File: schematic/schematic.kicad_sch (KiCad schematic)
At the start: 25 parts, among them SW1 SW_SPST, U1 ESP32-S3-DevKitC

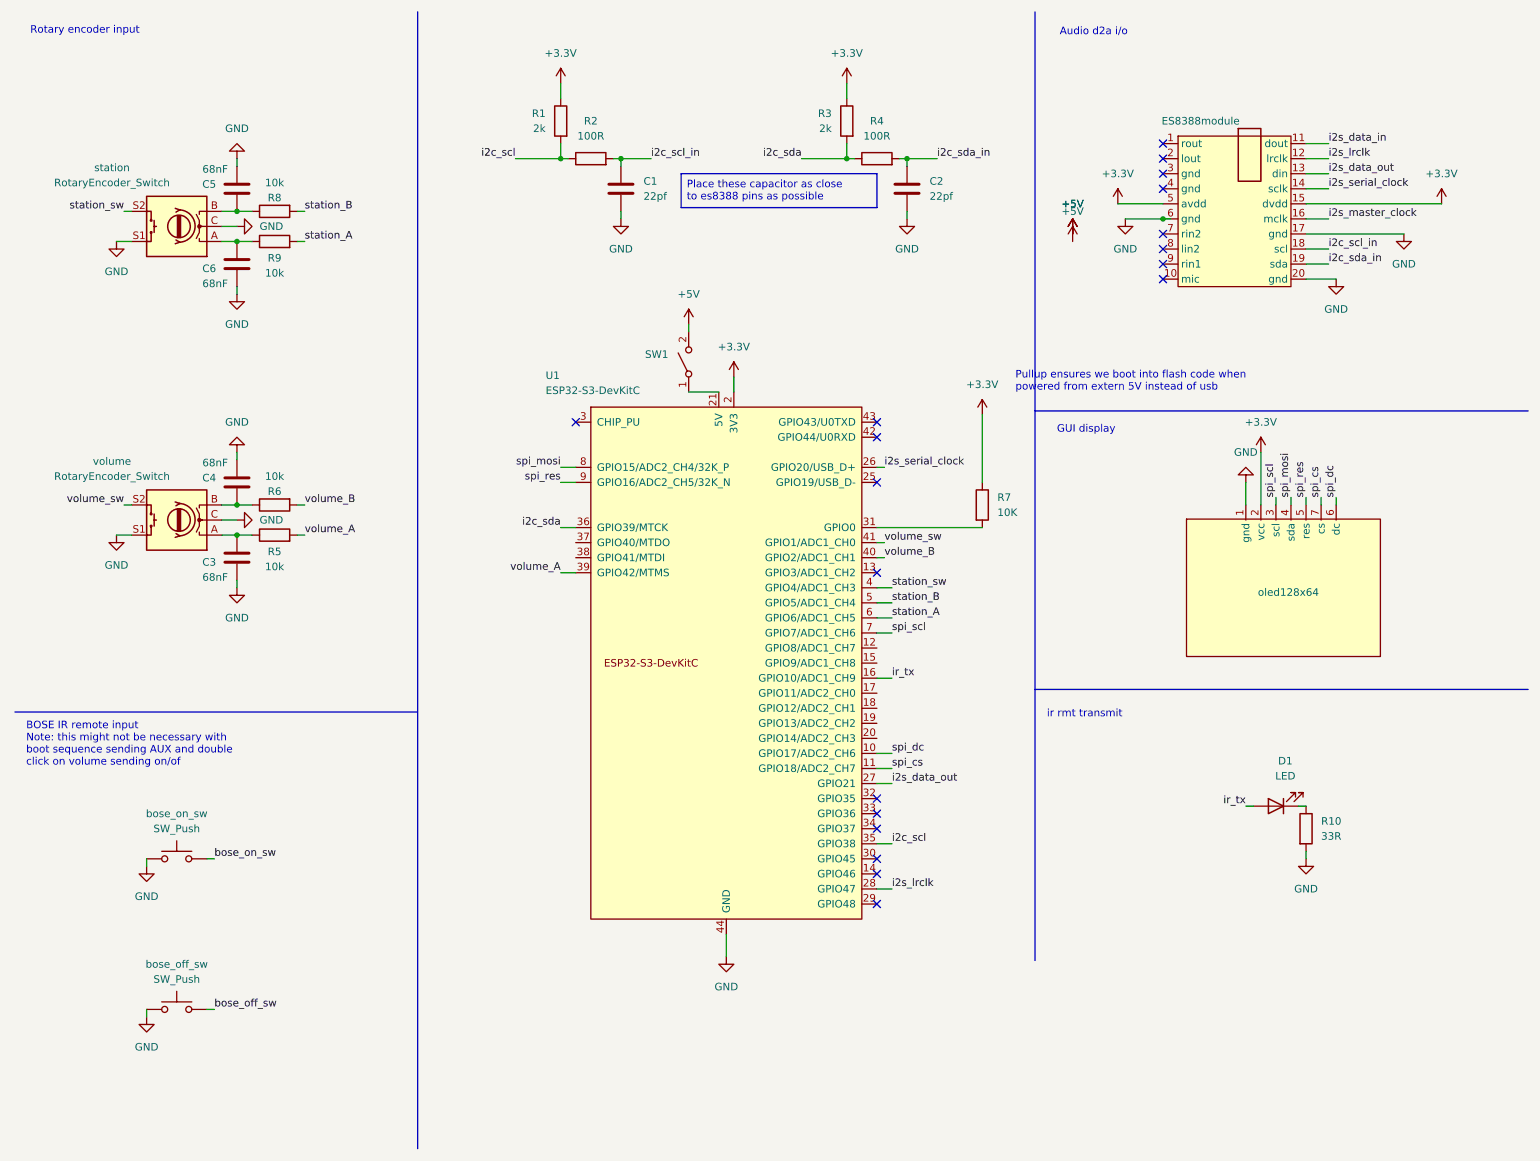
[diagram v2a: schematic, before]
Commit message: Assigned footprints and created custom footprints in prepartion for pcb layout.
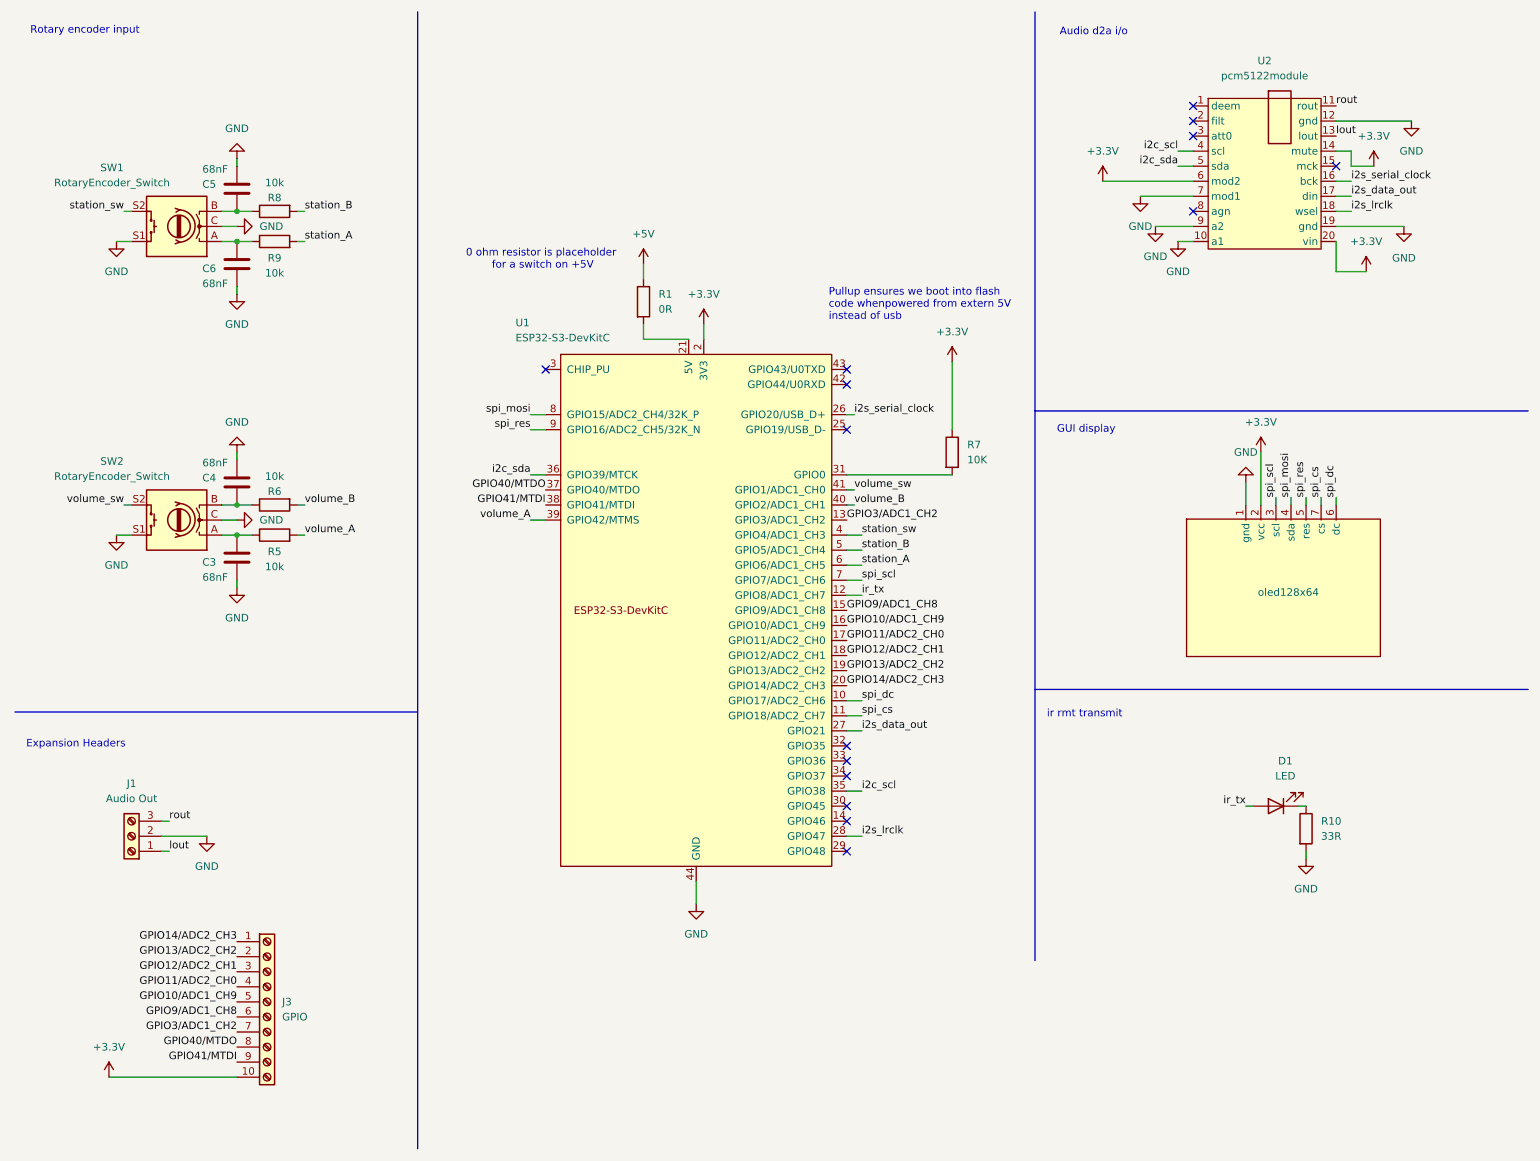
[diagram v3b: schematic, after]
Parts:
- removed C1, C2: 22pf, symbol Device:C
- removed ES8388module: ~, symbol es8388_module:es8388_module
- removed R2, R4: 100R, symbol Device:R
- removed R3: 2k, symbol Device:R
- removed SW1: SW_SPST, symbol Switch:SW_SPST
- removed bose_off_sw, bose_on_sw: SW_Push, symbol Switch:SW_Push
- added J1: Audio Out, TerminalBlock:TerminalBlock_Xinya_XY308-2.54-3P_1x03_P2.54mm_Horizontal, symbol Connector:Screw_Terminal_01x03
- added J3: GPIO, TerminalBlock:TerminalBlock_Xinya_XY308-2.54-10P_1x10_P2.54mm_Horizontal, symbol Connector:Screw_Terminal_01x10
- added U2: pcm5122module, symbol audio_boards:pcm5122
- C3, C4, C5, C6: footprint (none) -> Capacitor_SMD:C_1206_3216Metric_Pad1.33x1.80mm_HandSolder
- D1: footprint (none) -> LED_THT:LED_D3.0mm_IRGrey
- R1: value 2k -> 0R; footprint (none) -> Resistor_THT:R_Axial_DIN0207_L6.3mm_D2.5mm_P7.62mm_Horizontal
- R10, R5, R6, R7, R8, R9: footprint (none) -> Resistor_SMD:R_1206_3216Metric_Pad1.30x1.75mm_HandSolder
- SW1: renamed from station; footprint (none) -> rotary_encoder:XDCR_PEC11R-4220F-S0024
- SW2: renamed from volume; footprint (none) -> rotary_encoder:XDCR_PEC11R-4220F-S0024
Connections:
- net +3.3V: now also J3.10 (Pin_10), U2.14 (mute), U2.20 (vin), U2.6 (mod2); no longer R1.1
- net +5V: now also R1.1
- net GND: now also J1.2 (Pin_2), U2.10 (a1), U2.12 (gnd), U2.19 (gnd), U2.7 (mod1), U2.9 (a2)
- net i2c_scl: now also U2.4 (scl); no longer R1.2
- net i2c_sda: now also U2.5 (sda)
- net i2s_data_out: now also U2.17 (din)
- net i2s_lrclk: now also U2.18 (wsel)
- net i2s_serial_clock: now also U2.16 (bck)
- net ir_tx: now also U1.12 (GPIO8/ADC1_CH7); no longer U1.16 (GPIO10/ADC1_CH9)
- net at U1.21 (5V): now also R1.2
- net GPIO3/ADC1_CH2: now reaches U1.13 (GPIO3/ADC1_CH2)
- net GPIO3/ADC1_CH2: now also J3.7 (Pin_7)
- net GPIO9/ADC1_CH8: now reaches U1.15 (GPIO9/ADC1_CH8)
- net GPIO9/ADC1_CH8: now also J3.6 (Pin_6)
- net GPIO11/ADC2_CH0: now reaches U1.17 (GPIO11/ADC2_CH0)
- net GPIO11/ADC2_CH0: now also J3.4 (Pin_4)
- net GPIO12/ADC2_CH1: now reaches U1.18 (GPIO12/ADC2_CH1)
- net GPIO12/ADC2_CH1: now also J3.3 (Pin_3)
- net GPIO13/ADC2_CH2: now reaches U1.19 (GPIO13/ADC2_CH2)
- net GPIO13/ADC2_CH2: now also J3.2 (Pin_2)
- net GPIO14/ADC2_CH3: now reaches U1.20 (GPIO14/ADC2_CH3)
- net GPIO14/ADC2_CH3: now also J3.1 (Pin_1)
- net GPIO40/MTDO: now reaches U1.37 (GPIO40/MTDO)
- net GPIO40/MTDO: now also J3.8 (Pin_8)
- net GPIO41/MTDI: now reaches U1.38 (GPIO41/MTDI)
- net GPIO41/MTDI: now also J3.9 (Pin_9)
- new net GPIO10/ADC1_CH9: J3.5 (Pin_5), U1.16 (GPIO10/ADC1_CH9)
- new net lout: J1.1 (Pin_1), U2.13 (lout)
- new net rout: J1.3 (Pin_3), U2.11 (rout)
- no-connect marks 19 -> 15
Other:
- note added: "0 ohm resistor is placeholder for a switch on +5V"
- note added: "Expansion Headers"
- note added: "Pullup ensures we boot into flash code whenpowered from extern 5V instead of usb"
- note removed: "BOSE IR remote input Note: this might not be necessary with boot sequence sending AUX and double click on volume sending on/of"
- note removed: "Pullup ensures we boot into flash code when powered from extern 5V instead of usb"
- moved on the sheet: R7, U1

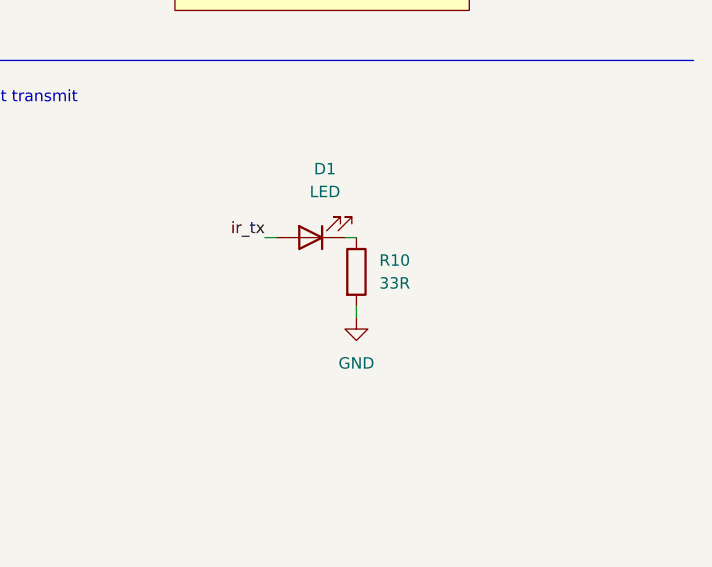
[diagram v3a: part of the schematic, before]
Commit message: Change current limiting resistor to 100R from 33R.  Lower power seems to work fine for the ir remote.
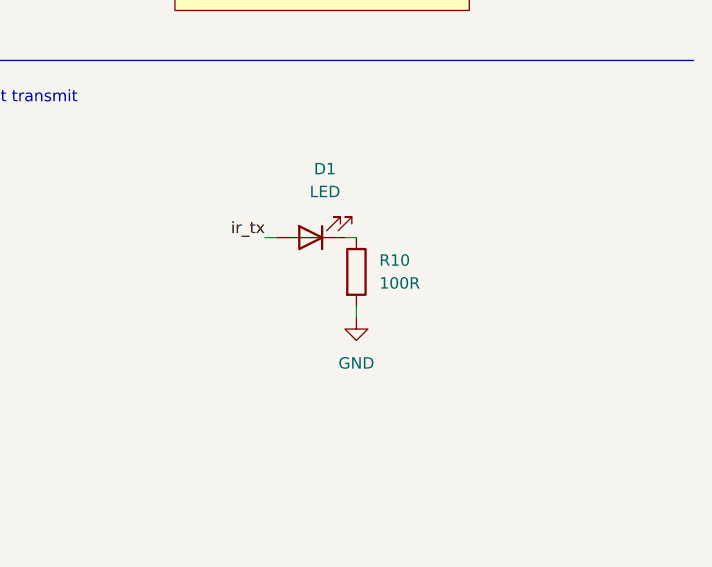
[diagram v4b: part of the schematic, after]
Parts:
- R10: value 33R -> 100R
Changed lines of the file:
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@@
 			)
 		)
-		(property "Value" "33R"
+		(property "Value" "100R"
 			(at 232.41 151.1299 0)
 			(effects

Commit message: Design PCB.
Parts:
- removed R1: 0R, Resistor_THT:R_Axial_DIN0207_L6.3mm_D2.5mm_P7.62mm_Horizontal, symbol Device:R
- removed R5, R6: 10k, Resistor_SMD:R_1206_3216Metric_Pad1.30x1.75mm_HandSolder, symbol Device:R
- removed SW1, SW2: RotaryEncoder_Switch, rotary_encoder:XDCR_PEC11R-4220F-S0024, symbol Device:RotaryEncoder_Switch
- added J3: Conn_01x02, Connector_Wire:SolderWire-0.1sqmm_1x02_P3.6mm_D0.4mm_OD1mm, symbol Connector_Generic:Conn_01x02
- added R3, R4: 10k, Resistor_SMD:R_0805_2012Metric_Pad1.20x1.40mm_HandSolder, symbol Device:R
- added S1, S2: PEC11R-4220F-S0024, rotary_encoder:XDCR_PEC11R-4220F-S0024, symbol rotary_encoder:PEC11R-4220F-S0024
- C1: renamed from C5; footprint Capacitor_SMD:C_1206_3216Metric_Pad1.33x1.80mm_HandSolder -> Capacitor_SMD:C_0805_2012Metric_Pad1.18x1.45mm_HandSolder
- C2: renamed from C6; footprint Capacitor_SMD:C_1206_3216Metric_Pad1.33x1.80mm_HandSolder -> Capacitor_SMD:C_0805_2012Metric_Pad1.18x1.45mm_HandSolder
- C3, C4: footprint Capacitor_SMD:C_1206_3216Metric_Pad1.33x1.80mm_HandSolder -> Capacitor_SMD:C_0805_2012Metric_Pad1.18x1.45mm_HandSolder
- R1: renamed from R8; footprint Resistor_SMD:R_1206_3216Metric_Pad1.30x1.75mm_HandSolder -> Resistor_SMD:R_0805_2012Metric_Pad1.20x1.40mm_HandSolder
- R2: renamed from R9; footprint Resistor_SMD:R_1206_3216Metric_Pad1.30x1.75mm_HandSolder -> Resistor_SMD:R_0805_2012Metric_Pad1.20x1.40mm_HandSolder
- R6: renamed from R7; footprint Resistor_SMD:R_1206_3216Metric_Pad1.30x1.75mm_HandSolder -> Resistor_SMD:R_0805_2012Metric_Pad1.20x1.40mm_HandSolder
- R7: renamed from R10; footprint Resistor_SMD:R_1206_3216Metric_Pad1.30x1.75mm_HandSolder -> Resistor_SMD:R_0805_2012Metric_Pad1.20x1.40mm_HandSolder
- U2: footprint (none) -> audio_boards:pcm5122_module
- oled128x1: renamed from oled128x64; footprint (none) -> oled128x64_spi:oled128x64_spi
- renumbered J3 to J2
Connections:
- net GND: now also J3.2 (Pin_2), S1.1, S1.C (COM), S1.SH1 (SHIELD), S1.SH2 (SHIELD__1), S2.1, S2.C (COM), S2.SH1 (SHIELD), S2.SH2 (SHIELD__1)
- net station_A: now also R1.2, U1.5 (GPIO5/ADC1_CH4); no longer R2.2, U1.6 (GPIO6/ADC1_CH5)
- net station_B: now also R2.2, U1.4 (GPIO4/ADC1_CH3); no longer R1.2, U1.5 (GPIO5/ADC1_CH4)
- net station_sw: now also U1.6 (GPIO6/ADC1_CH5), S1.2; no longer U1.4 (GPIO4/ADC1_CH3)
- net volume_A: now also R3.2
- net volume_B: now also R4.2
- net volume_sw: now also S2.2
- net at U1.21 (5V): now also J3.1 (Pin_1)
- net at C4.1: now also R4.1, S2.B
- net at C2.1, R2.1: now also S1.B
- net at C1.1, R1.1: now also S1.A
- net at C3.1: now also R3.1, S2.A
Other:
- moved on the sheet: C1, C2, R1, R2

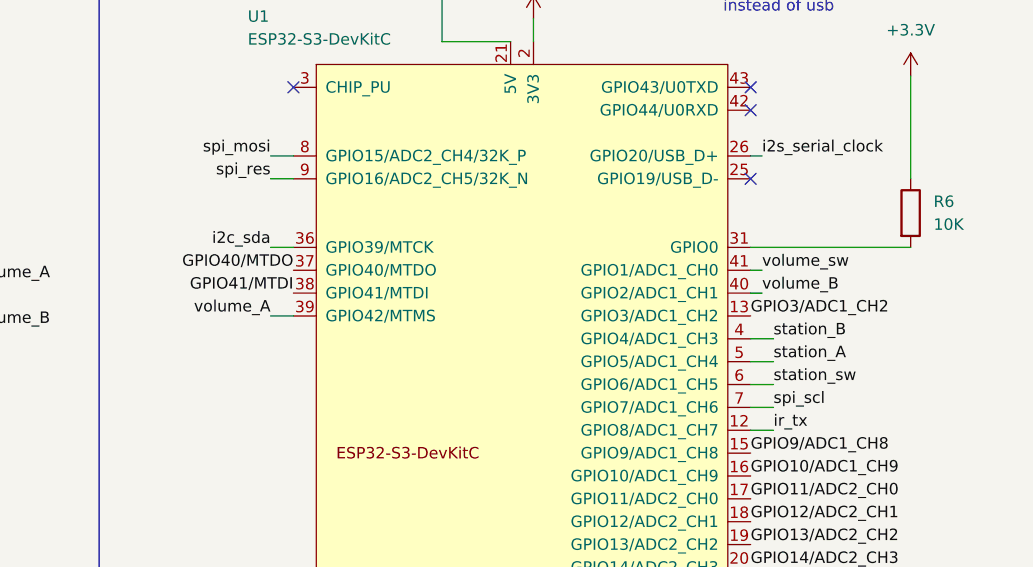
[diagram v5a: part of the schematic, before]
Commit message: Reassigned volume encoder pins in order to reroute outside of the esp32 antenna.  Also added a keep out zone on both top and bottom around the antenna.
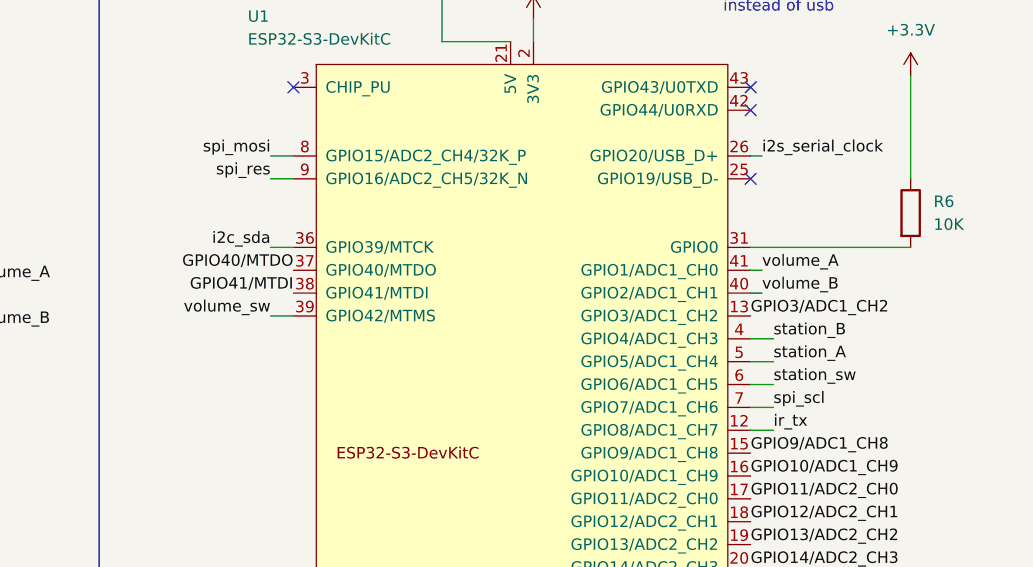
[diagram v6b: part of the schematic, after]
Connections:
- net volume_A: now also U1.41 (GPIO1/ADC1_CH0); no longer U1.39 (GPIO42/MTMS)
- net volume_sw: now also U1.39 (GPIO42/MTMS); no longer U1.41 (GPIO1/ADC1_CH0)
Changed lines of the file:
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@@
-		)
-	)
-	(label "volume_A"
-		(at 99.06 97.79 180)
-		(effects
-			(font
-				(size 1.27 1.27)
-			)
-			(justify right bottom)
 		)
 	)
@@
 		)
 	)
+	(label "volume_A"
+		(at 153.67 92.71 0)
+		(effects
+			(font
+				(size 1.27 1.27)
+			)
+			(justify left bottom)
+		)
+	)
 	(label "GPIO11/ADC2_CH0"
 		(at 152.4 118.11 0)
@@
 	)
 	(label "volume_sw"
-		(at 153.67 92.71 0)
-		(effects
-			(font
-				(size 1.27 1.27)
-			)
-			(justify left bottom)
-		)
-	)
+		(at 99.06 97.79 180)
+		(effects
+			(font
+				(size 1.27 1.27)
+			)
+			(justify right bottom)
+		)
+	)

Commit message: moved to kicad 10
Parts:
- oled128x1: value ~ -> (none)

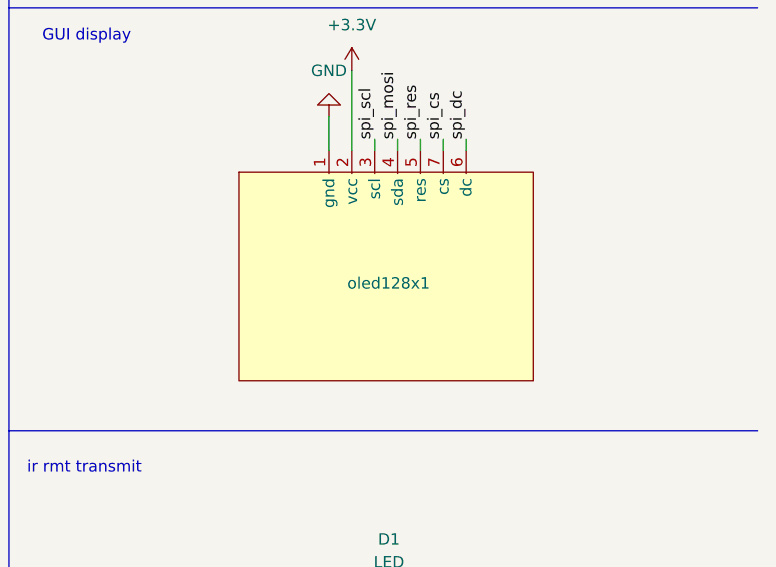
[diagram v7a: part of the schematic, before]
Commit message: fix spelling in schematic.
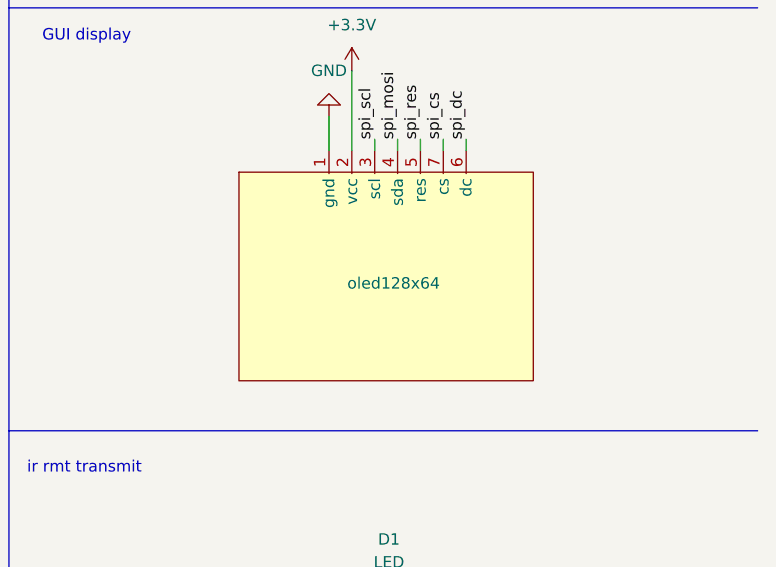
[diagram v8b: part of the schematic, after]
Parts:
- renumbered oled128x1 to oled128x64
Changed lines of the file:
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@@
 		(in_pos_files yes)
 		(dnp no)
-		(property "Reference" "oled128x1"
+		(property "Reference" "oled128x64"
 			(at 221.742 109.982 0)
 			(show_name no)
@@
 			(project "schematic"
 				(path "/ad99cfc7-1930-4a76-846f-3ad4dbd23fae"
-					(reference "oled128x1")
+					(reference "oled128x64")
 					(unit 1)
 				)
